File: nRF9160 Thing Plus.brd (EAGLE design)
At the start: 58.4 x 22.9 mm, 123 parts, among them J1 USB Female C, J10 QWIIC_RIGHT_ANGLE, J2 CON-HEADER-1X12-MALE-PIN, J3 CON-HEADER-1X16-MALE-PIN, J4 CON-1909763-1, J6 CON-SIM-104224-0820, J7 CON-1909763-1, J8 CON-FTSH-105-XX-X-DV, Q1 MOSFET-P-SC89, Q2 MOSFET-DUAL-COMP-SOT563, Q3 MOSFET-P-20V-4.7A-SOT23, Q4 MOSFET-N-SC89, Q5 MOSFET-N-SC89, SW1 MOMENTARY-SWITCH-SPST-SMD-4.6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, SW2 MOMENTARY-SWITCH-SPST-SMD-4.6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, U1 MOD-NRF9160-SICA-R, U12 IC-LIS2DH12TR, U2 MCP73831, U3 IC-TPS63031DSKR, U4 POWER-SWITCH-MIC94092YC6, U5 IC-CP2102N-A02-GQFN24R, U6 FLASH-W25Q128JVPIM-WSON, U8 IC-PCF85063ATL/1, U9 IC-BAV70S, Y1 XTAL-ABS07AIG-32.768KHZ-7-T

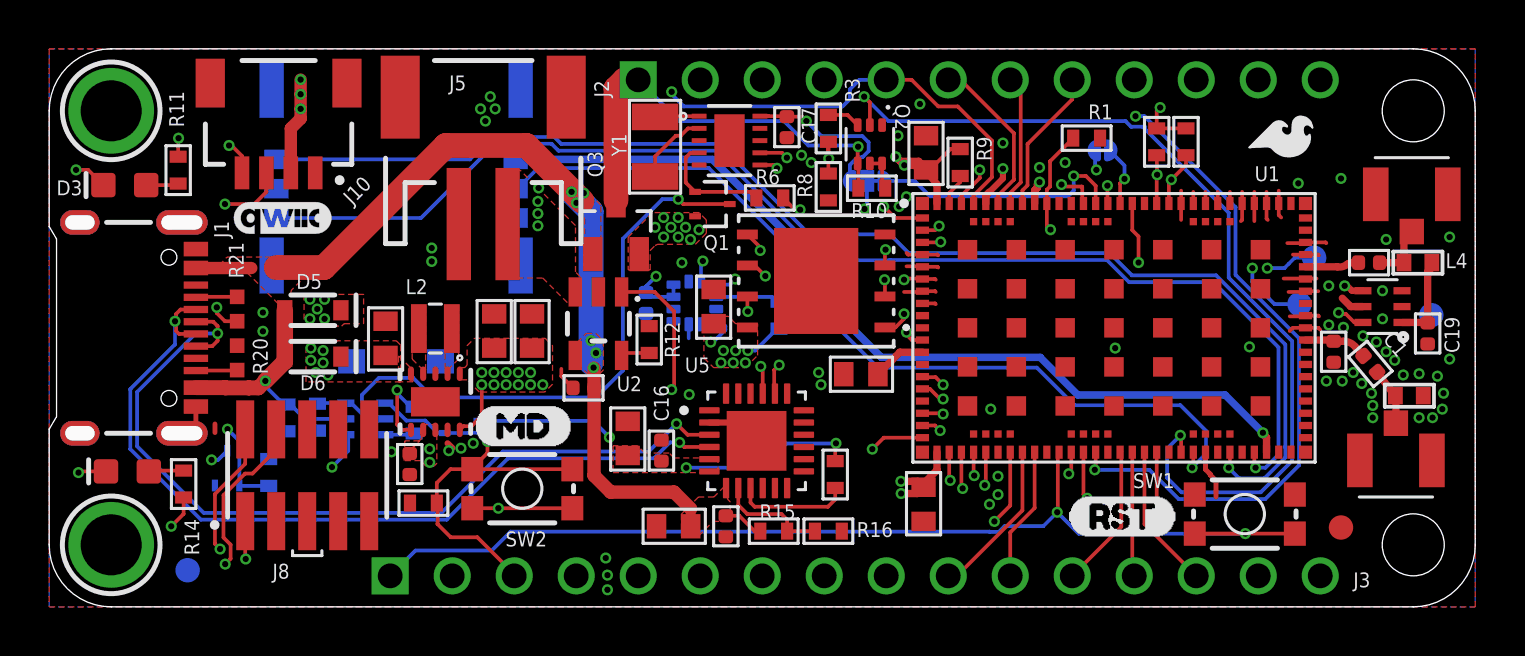
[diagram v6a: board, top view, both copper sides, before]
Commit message: Changing flash to W25Q32JVZPIQ. Changing D5/6 to BAT20J.
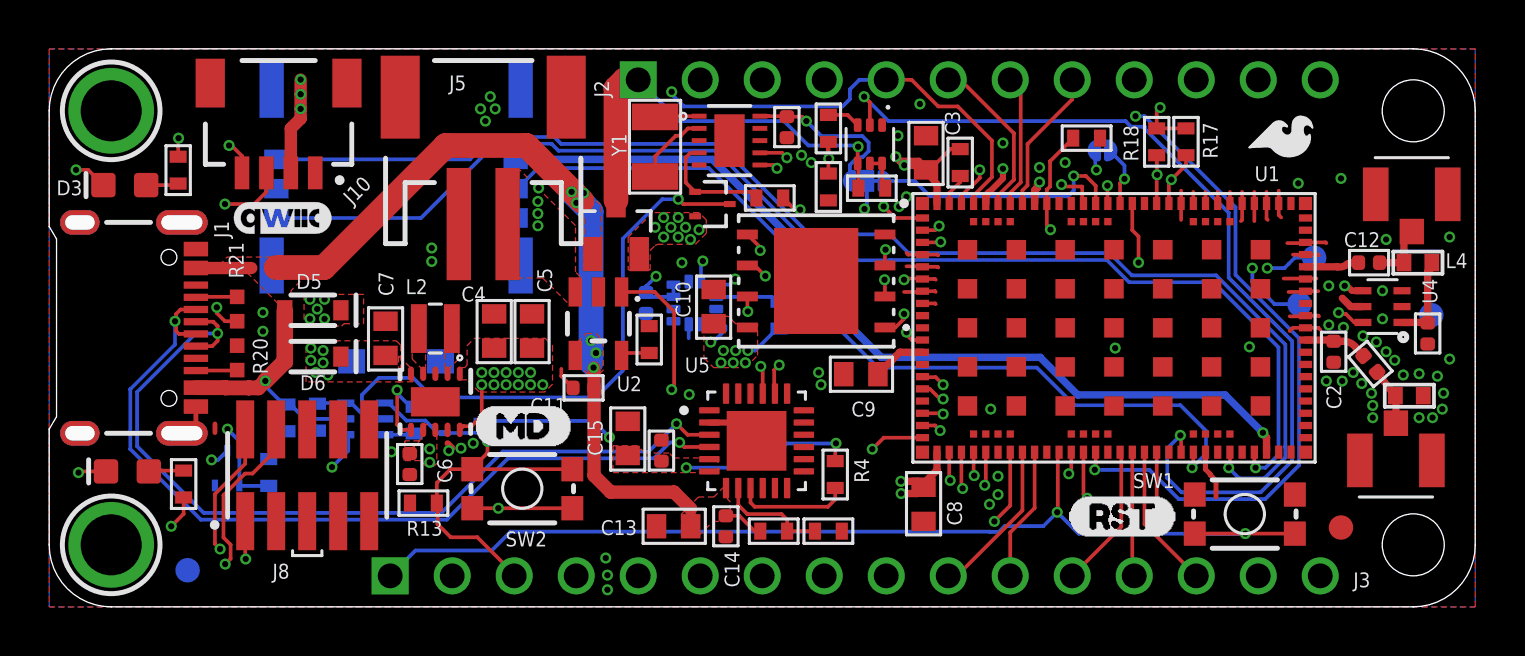
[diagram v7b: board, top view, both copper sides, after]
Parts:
- D5, D6: value 3A/10V/280mV -> 1A/23V/620mV
- U6: value FLASH-W25Q128JVPIM-WSON -> FLASH-WSON; device nRF9160-IC:WIN_ZP-8-L -> wolff-den:WIN_ZP-8-L

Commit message: Adding test points for SIM
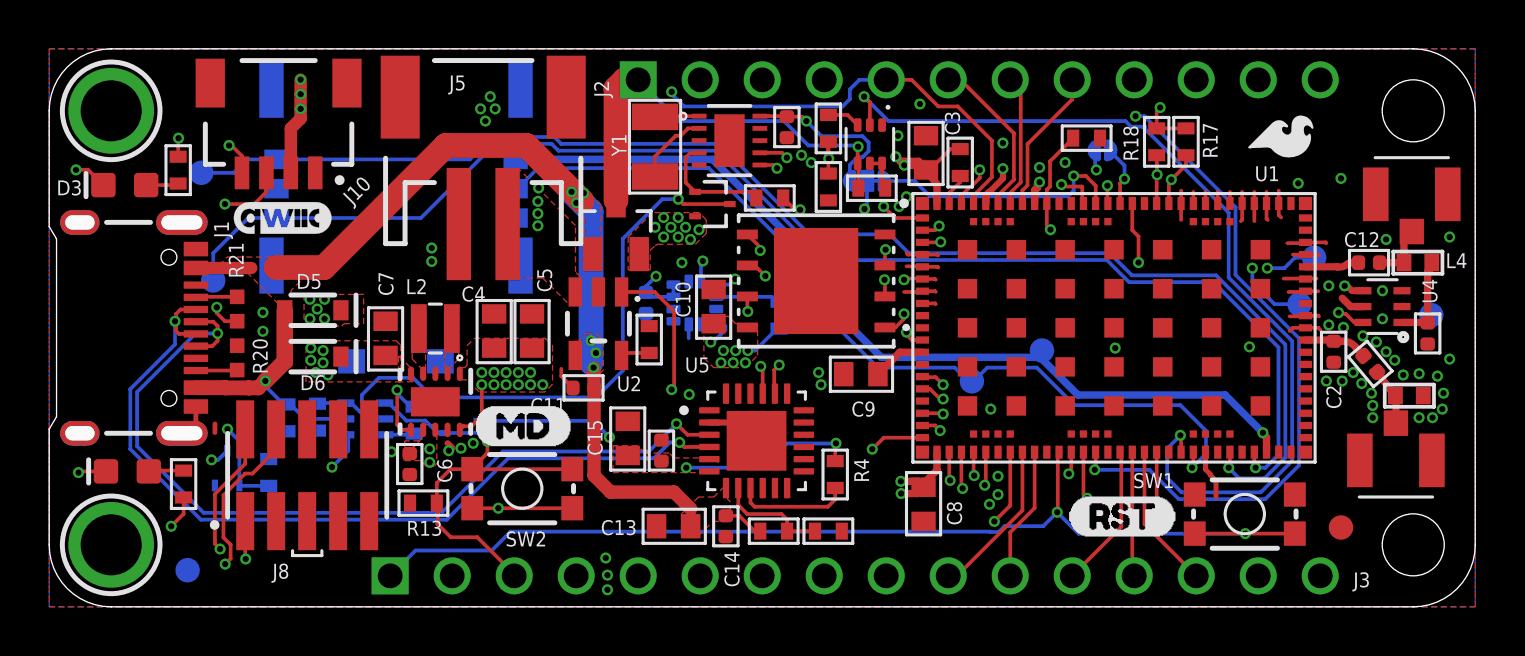
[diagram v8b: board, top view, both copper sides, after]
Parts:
- added TP3, TP4, TP5, TP6: TP-1SIDE-1P0, wolff-den:TP-1P0
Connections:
- net SIM_CLK: now also TP3.TP
- net SIM_IO: now also TP6.TP
- net SIM_RST: now also TP4.TP
- net SIM_VCC: now also TP5.TP
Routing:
- net SIM_IO: track 52.0 -> 56.3 mm
- net SIM_CLK: track 53.4 -> 56.7 mm
- net SIM_RST: track 36.2 -> 36.7 mm
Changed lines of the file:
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@@
 <grid distance="0.07" unitdist="mm" unit="mm" style="lines" multiple="1" display="yes" altdistance="0.005" altunitdist="inch" altunit="inch"/>
 <layers>
-<layer number="1" name="Top" color="4" fill="1" visible="yes" active="yes"/>
-<layer number="16" name="Bottom" color="1" fill="1" visible="no" active="yes"/>
+<layer number="1" name="Top" color="4" fill="1" visible="no" active="yes"/>
+<layer number="16" name="Bottom" color="1" fill="1" visible="yes" active="yes"/>
 <layer number="17" name="Pads" color="2" fill="1" visible="yes" active="yes"/>
 <layer number="18" name="Vias" color="2" fill="1" visible="yes" active="yes"/>
 <layer number="19" name="Unrouted" color="6" fill="1" visible="yes" active="yes"/>
 <layer number="20" name="Dimension" color="24" fill="1" visible="yes" active="yes"/>
-<layer number="21" name="tPlace" color="16" fill="1" visible="yes" active="yes"/>
-<layer number="22" name="bPlace" color="14" fill="1" visible="no" active="yes"/>
-<layer number="23" name="tOrigins" color="15" fill="1" visible="yes" active="yes"/>
-<layer number="24" name="bOrigins" color="15" fill="1" visible="no" active="yes"/>
-<layer number="25" name="tNames" color="7" fill="1" visible="yes" active="yes"/>
-<layer number="26" name="bNames" color="7" fill="1" visible="no" active="yes"/>
+<layer number="21" name="tPlace" color="16" fill="1" visible="no" active="yes"/>
+<layer number="22" name="bPlace" color="14" fill="1" visible="yes" active="yes"/>
+<layer number="23" name="tOrigins" color="15" fill="1" visible="no" active="yes"/>
+<layer number="24" name="bOrigins" color="15" fill="1" visible="yes" active="yes"/>
+<layer number="25" name="tNames" color="7" fill="1" visible="no" active="yes"/>
+<layer number="26" name="bNames" color="7" fill="1" visible="yes" active="yes"/>
 <layer number="27" name="tValues" color="7" fill="1" visible="no" active="yes"/>
 <layer number="28" name="bValues" color="7" fill="1" visible="no" active="yes"/>
@@
 <layer number="37" name="tTest" color="7" fill="1" visible="no" active="yes"/>
 <layer number="38" name="bTest" color="7" fill="1" visible="no" active="yes"/>
-<layer number="39" name="tKeepout" color="4" fill="11" visible="yes" active="yes"/>
-<layer number="40" name="bKeepout" color="1" fill="11" visible="no" active="yes"/>
-<layer number="41" name="tRestrict" color="4" fill="10" visible="yes" active="yes"/>
-<layer number="42" name="bRestrict" color="1" fill="10" visible="no" active="yes"/>
+<layer number="39" name="tKeepout" color="4" fill="11" visible="no" active="yes"/>
+<layer number="40" name="bKeepout" color="1" fill="11" visible="yes" active="yes"/>
+<layer number="41" name="tRestrict" color="4" fill="10" visible="no" active="yes"/>
+<layer number="42" name="bRestrict" color="1" fill="10" visible="yes" active="yes"/>
 <layer number="43" name="vRestrict" color="2" fill="10" visible="no" active="yes"/>
 <layer number="44" name="Drills" color="7" fill="1" visible="no" active="yes"/>
@@
 <attribute name="PRICE" value="None" x="2.31" y="4.9" size="1.778" layer="28" rot="MR180" display="off"/>
 </element>
+<element name="TP3" library="wolff-den" library_urn="urn:adsk.eagle:library:6370453" package="TP-1P0" package3d_urn="urn:adsk.eagle:package:24898411/1" value="TP-1SIDE-1P0" x="6.23" y="17.78" smashed="yes" rot="MR0">
+<attribute name="NAME" x="5.32" y="17.5" size="0.6096" layer="26" font="vector" ratio="20" rot="MR0"/>
+</element>
+<element name="TP4" library="wolff-den" library_urn="urn:adsk.eagle:library:6370453" package="TP-1P0" package3d_urn="urn:adsk.eagle:package:24898411/1" value="TP-1SIDE-1P0" x="37.8" y="9.24" smashed="yes" rot="MR0">
+<attribute name="NAME" x="38.435" y="10.256" size="0.6096" layer="26" font="vector" ratio="20" rot="MR0"/>
+</element>
+<element name="TP5" library="wolff-den" library_urn="urn:adsk.eagle:library:6370453" package="TP-1P0" package3d_urn="urn:adsk.eagle:package:24898411/1" value="TP-1SIDE-1P0" x="40.67" y="10.5" smashed="yes" rot="MR0">
+<attribute name="NAME" x="41.305" y="11.516" size="0.6096" layer="26" font="vector" ratio="20" rot="MR0"/>
+</element>
+<element name="TP6" library="wolff-den" library_urn="urn:adsk.eagle:library:6370453" package="TP-1P0" package3d_urn="urn:adsk.eagle:package:24898411/1" value="TP-1SIDE-1P0" x="6.72" y="13.37" smashed="yes" rot="MR270">
+<attribute name="NAME" x="4.335" y="13.054" size="0.6096" layer="26" font="vector" ratio="20" rot="MR180"/>
+</element>
 </elements>
 <signals>
@@
 <wire x1="44.3557375" y1="13.5794" x2="47.8054625" y2="13.5794" width="0.1524" layer="16"/>
 <wire x1="47.8054625" y1="13.5794" x2="50.64" y2="10.7448625" width="0.1524" layer="16"/>
-<wire x1="50.64" y1="10.7448625" x2="50.64" y2="6.58" width="0.1524" layer="16"/>
-<wire x1="50.64" y1="6.5151375" x2="50.64" y2="6.58" width="0.1524" layer="16"/>
-<wire x1="50.64" y1="6.5151375" x2="50.64" y2="6.12" width="0.1524" layer="16"/>
+<wire x1="50.64" y1="10.7448625" x2="50.64" y2="6.12" width="0.1524" layer="16"/>
 <wire x1="50.64" y1="6.12" x2="49.7882" y2="5.2682" width="0.1524" layer="16"/>
 <wire x1="48.7411375" y1="5.2682" x2="48.32" y2="5.6893375" width="0.1524" layer="16"/>
 <wire x1="49.7882" y1="5.2682" x2="48.7411375" y2="5.2682" width="0.1524" layer="16"/>
+<contactref element="TP3" pad="TP"/>
+<wire x1="6.23" y1="17.78" x2="7.57" y2="17.78" width="0.1524" layer="16"/>
+<wire x1="8.12" y1="18.33" x2="9.31" y2="18.33" width="0.1524" layer="16"/>
+<wire x1="8.12" y1="18.33" x2="7.57" y2="17.78" width="0.1524" layer="16"/>
 </signal>
 <signal name="SIM_RST">
@@
 <wire x1="47.39" y1="6.27" x2="47.39" y2="7.21" width="0.1524" layer="16"/>
 <wire x1="42" y1="8.26" x2="40.46" y2="9.8" width="0.1524" layer="16"/>
-<wire x1="40.46" y1="9.8" x2="33.95" y2="9.8" width="0.1524" layer="16"/>
-<wire x1="33.95" y1="9.8" x2="32.13" y2="11.62" width="0.1524" layer="16"/>
+<wire x1="32.13" y1="11.62" x2="33.95" y2="9.8" width="0.1524" layer="16"/>
 <wire x1="27.0227" y1="17.9744" x2="20.0244" y2="17.9744" width="0.1524" layer="16"/>
+<contactref element="TP4" pad="TP"/>
+<wire x1="40.46" y1="9.8" x2="38.43" y2="9.8" width="0.1524" layer="16"/>
+<wire x1="38.43" y1="9.8" x2="37.975" y2="9.345" width="0.1524" layer="16"/>
+<wire x1="37.975" y1="9.345" x2="37.905" y2="9.345" width="0.1524" layer="16"/>
+<wire x1="37.8" y1="9.24" x2="37.73" y2="9.17" width="0.1524" layer="16"/>
+<wire x1="37.905" y1="9.345" x2="37.8" y2="9.24" width="0.1524" layer="16"/>
+<wire x1="33.95" y1="9.8" x2="37.1" y2="9.8" width="0.1524" layer="16"/>
+<wire x1="37.1" y1="9.8" x2="37.73" y2="9.17" width="0.1524" layer="16"/>
 </signal>
 <signal name="SIM_IO">
@@
 <wire x1="50.3606" y1="10.629125" x2="47.689725" y2="13.3" width="0.1524" layer="16"/>
 <wire x1="47.689725" y1="13.3" x2="44.24" y2="13.3" width="0.1524" layer="16"/>
+<contactref element="TP6" pad="TP"/>
+<wire x1="6.72" y1="14.49" x2="6.72" y2="13.37" width="0.1524" layer="16"/>
+<wire x1="6.72" y1="14.49" x2="8.16" y2="15.93" width="0.1524" layer="16"/>
+<wire x1="8.16" y1="15.93" x2="9.31" y2="15.93" width="0.1524" layer="16"/>
 </signal>
 <signal name="SIM_VCC">
@@
 <via x="49.72" y="7.1318" extent="1-16" drill="0.254"/>
 <contactref element="J6" pad="S1"/>
-<wire x1="40.6" y1="10.22" x2="34.09" y2="10.22" width="0.3048" layer="16"/>
-<wire x1="34.09" y1="10.22" x2="32.55" y2="11.76" width="0.3048" layer="16"/>
+<wire x1="32.55" y1="11.76" x2="34.09" y2="10.22" width="0.3048" layer="16"/>
 <wire x1="27.17" y1="18.33" x2="19.11" y2="18.33" width="0.3048" layer="16"/>
 <wire x1="49.72" y1="7.1318" x2="48.1718" y2="8.68" width="0.3048" layer="16"/>
 <wire x1="48.1718" y1="8.68" x2="42.14" y2="8.68" width="0.3048" layer="16"/>
-<wire x1="42.14" y1="8.68" x2="40.6" y2="10.22" width="0.3048" layer="16"/>
 <wire x1="32.55" y1="11.76" x2="32.55" y2="12.95" width="0.3048" layer="16"/>
 <wire x1="32.55" y1="12.95" x2="27.17" y2="18.33" width="0.3048" layer="16"/>
+<contactref element="TP5" pad="TP"/>
+<wire x1="42.14" y1="8.68" x2="40.67" y2="10.15" width="0.3048" layer="16"/>
+<wire x1="40.67" y1="10.15" x2="40.67" y2="10.5" width="0.3048" layer="16"/>
+<wire x1="34.09" y1="10.22" x2="40.39" y2="10.22" width="0.3048" layer="16"/>
+<wire x1="40.39" y1="10.22" x2="40.67" y2="10.5" width="0.3048" layer="16"/>
 </signal>
 <signal name="ANT_FILT" class="2">
